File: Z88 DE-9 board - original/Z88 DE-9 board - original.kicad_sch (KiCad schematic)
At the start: 12 parts, among them J1 DE-9 PCB Mount, J2 D header

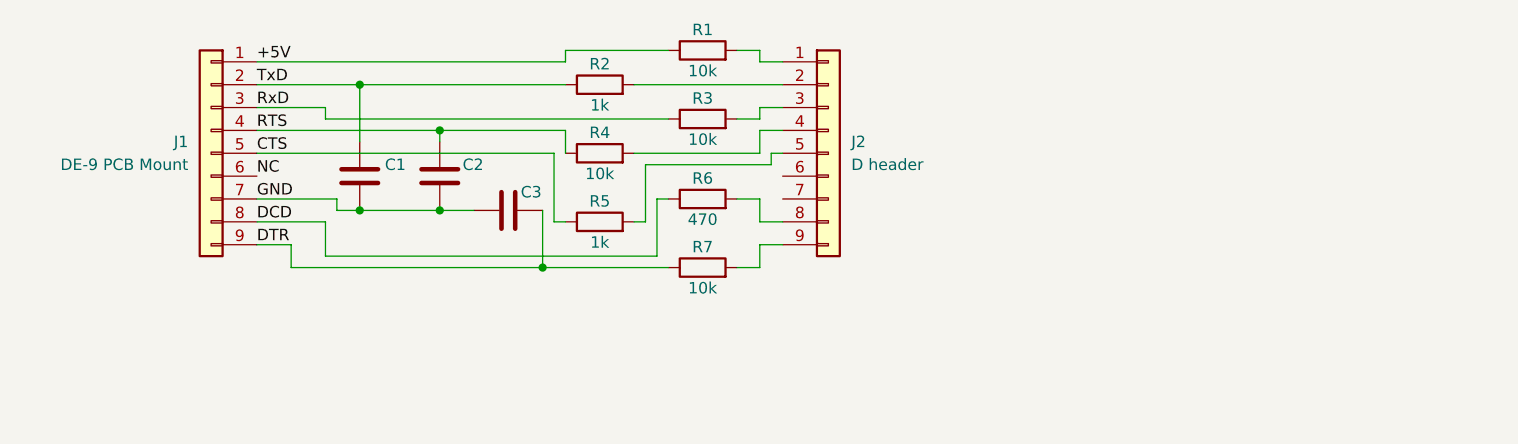
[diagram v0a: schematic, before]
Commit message: changed single-row header to dual so IDC connector can be used, replaced DE-9 footprint with custom to remove overhanging silkscreen
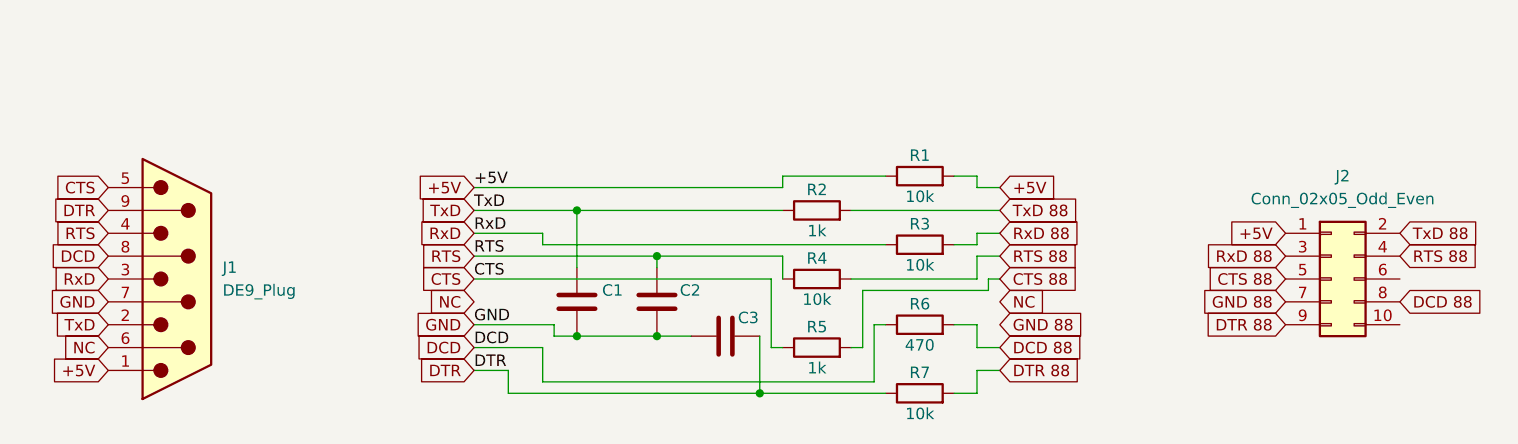
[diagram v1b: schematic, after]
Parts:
- removed J1: DE-9 PCB Mount, Connector_Dsub:DSUB-9_Female_Vertical_P2.77x2.84mm, symbol Connector_Generic:Conn_01x09
- removed J2: D header, Connector_PinHeader_2.54mm:PinHeader_1x09_P2.54mm_Vertical, symbol Connector_Generic:Conn_01x09
- added J1: DE9_Plug, DE-9:DE-9_Female_Vertical, symbol Connector:DE9_Plug
- added J2: Conn_02x05_Odd_Even, Connector_PinHeader_2.54mm:PinHeader_2x05_P2.54mm_Vertical, symbol Connector_Generic:Conn_02x05_Odd_Even
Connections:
- net +5V: now also R1.2, J1.1, J2.1 (Pin_1)
- net CTS: now also J1.5
- net DCD: now also J1.8
- net DTR: now also J1.9
- net GND: now also J1.7
- net NC: now also J1.6
- net RTS: now also J1.4
- net RxD: now also J1.3
- net TxD: now also J1.2
- net TxD 88: now reaches R2.2
- net TxD 88: now also J2.2 (Pin_2)
- net RxD 88: now reaches R3.2
- net RxD 88: now also J2.3 (Pin_3)
- net CTS 88: now reaches R5.2
- net CTS 88: now also J2.5 (Pin_5)
- net DTR 88: now reaches R7.2
- net DTR 88: now also J2.9 (Pin_9)
- net RTS 88: now reaches R4.2
- net RTS 88: now also J2.4 (Pin_4)
- net DCD 88: now reaches R6.2
- net DCD 88: now also J2.8 (Pin_8)
- new net GND 88: J2.7 (Pin_7)
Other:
- moved on the sheet: C1, C2, C3, R1, R2, R3, R4, R5, R6, R7

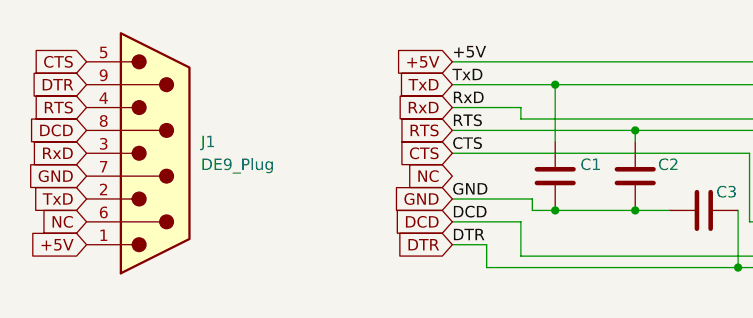
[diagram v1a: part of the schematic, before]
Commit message: minor schematic tweaks
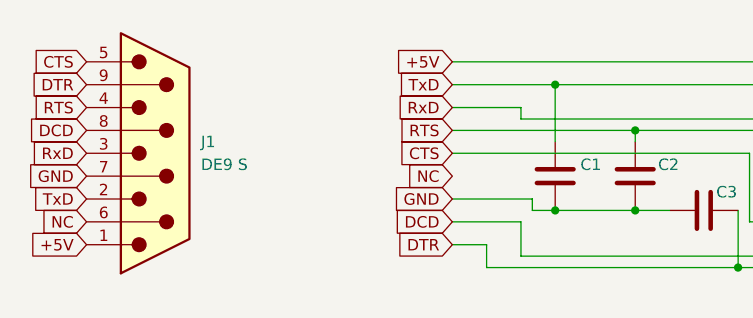
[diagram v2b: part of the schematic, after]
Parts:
- J1: value DE9_Plug -> DE9 S
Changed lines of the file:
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@@
 (kicad_sch
-	(version 20231120)
+	(version 20250114)
 	(generator "eeschema")
-	(generator_version "8.0")
+	(generator_version "9.0")
 	(paper "A4")
 	(junction
@@
 			(width 0)
 			(type default)
-		)
-	)
-	(label "RxD"
-		(at 119.38 96.52 0)
-		(fields_autoplaced yes)
-		(effects
-			(font
-				(size 1.27 1.27)
-			)
-			(justify left bottom)
-		)
-	)
-	(label "DTR"
-		(at 119.38 111.76 0)
-		(fields_autoplaced yes)
-		(effects
-			(font
-				(size 1.27 1.27)
-			)
-			(justify left bottom)
-		)
-	)
-	(label "GND"
-		(at 119.38 106.68 0)
-		(fields_autoplaced yes)
-		(effects
-			(font
-				(size 1.27 1.27)
-			)
-			(justify left bottom)
-		)
-	)
-	(label "DCD"
-		(at 119.38 109.22 0)
-		(fields_autoplaced yes)
-		(effects
-			(font
-				(size 1.27 1.27)
-			)
-			(justify left bottom)
-		)
-	)
-	(label "CTS"
-		(at 119.38 101.6 0)
-		(fields_autoplaced yes)
-		(effects
-			(font
-				(size 1.27 1.27)
-			)
-			(justify left bottom)
-		)
-	)
-	(label "TxD"
-		(at 119.38 93.98 0)
-		(fields_autoplaced yes)
-		(effects
-			(font
-				(size 1.27 1.27)
-			)
-			(justify left bottom)
-		)
-	)
-	(label "RTS"
-		(at 119.38 99.06 0)
-		(fields_autoplaced yes)
-		(effects
-			(font
-				(size 1.27 1.27)
-			)
-			(justify left bottom)
-		)
-	)
-	(label "+5V"
-		(at 119.38 91.44 0)
-		(fields_autoplaced yes)
-		(effects
-			(font
-				(size 1.27 1.27)
-			)
-			(justify left bottom)
 		)
 	)
@@
 			)
 		)
-		(property "Value" "DE9_Plug"
+		(property "Value" "DE9 S"
 			(at 91.44 102.8699 0)
 			(effects
@@
 		)
 	)
+	(embedded_fonts no)
 )
